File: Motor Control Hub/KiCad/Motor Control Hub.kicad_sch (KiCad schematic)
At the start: 6 parts, among them J2 GPIO, J3 Voltage Supply, J4 Motor Controllers

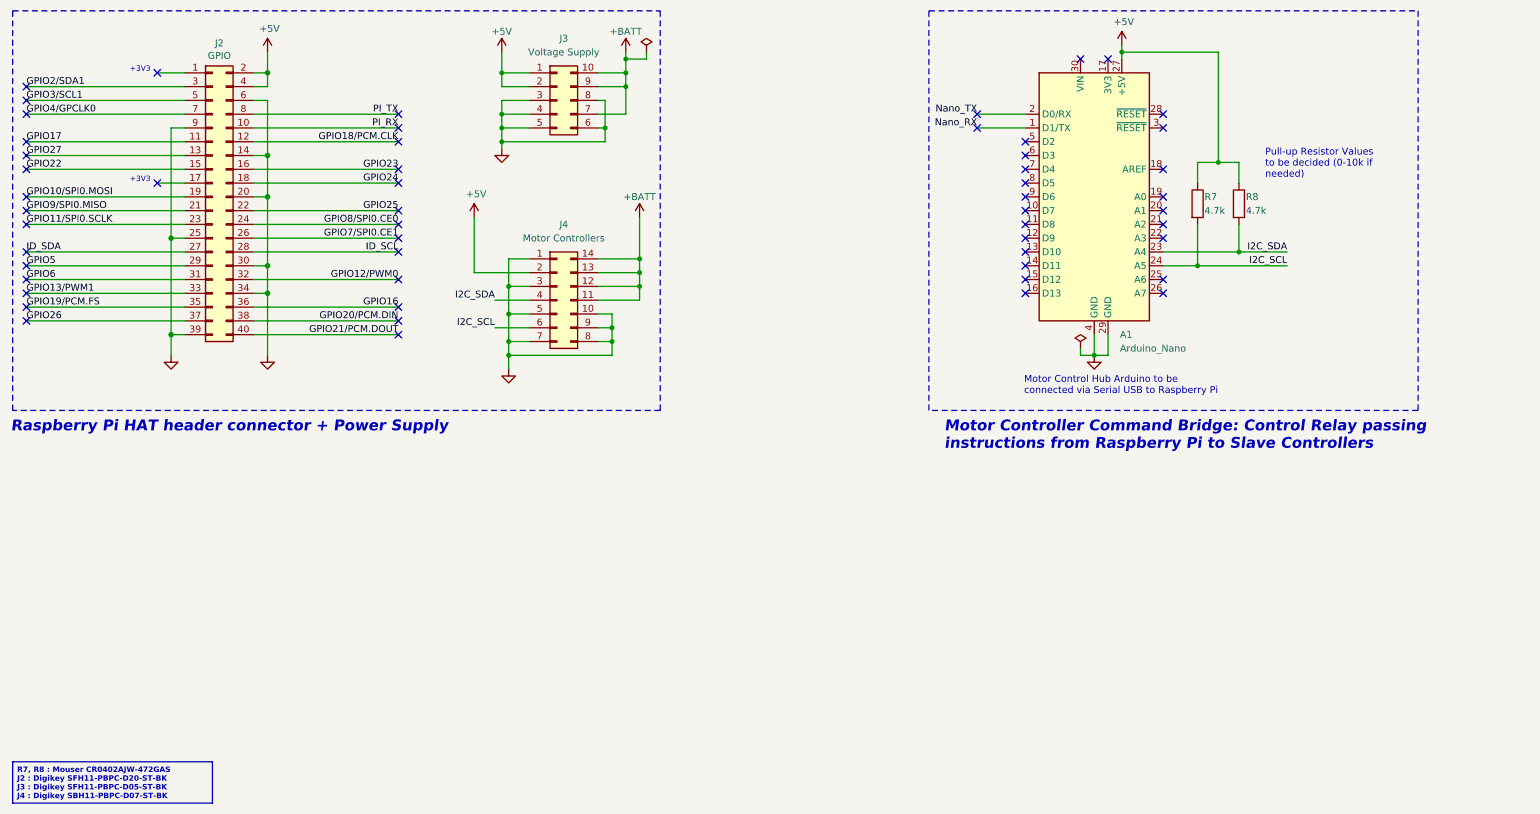
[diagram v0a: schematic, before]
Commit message: added encoders, slightly adjusted copper tracks
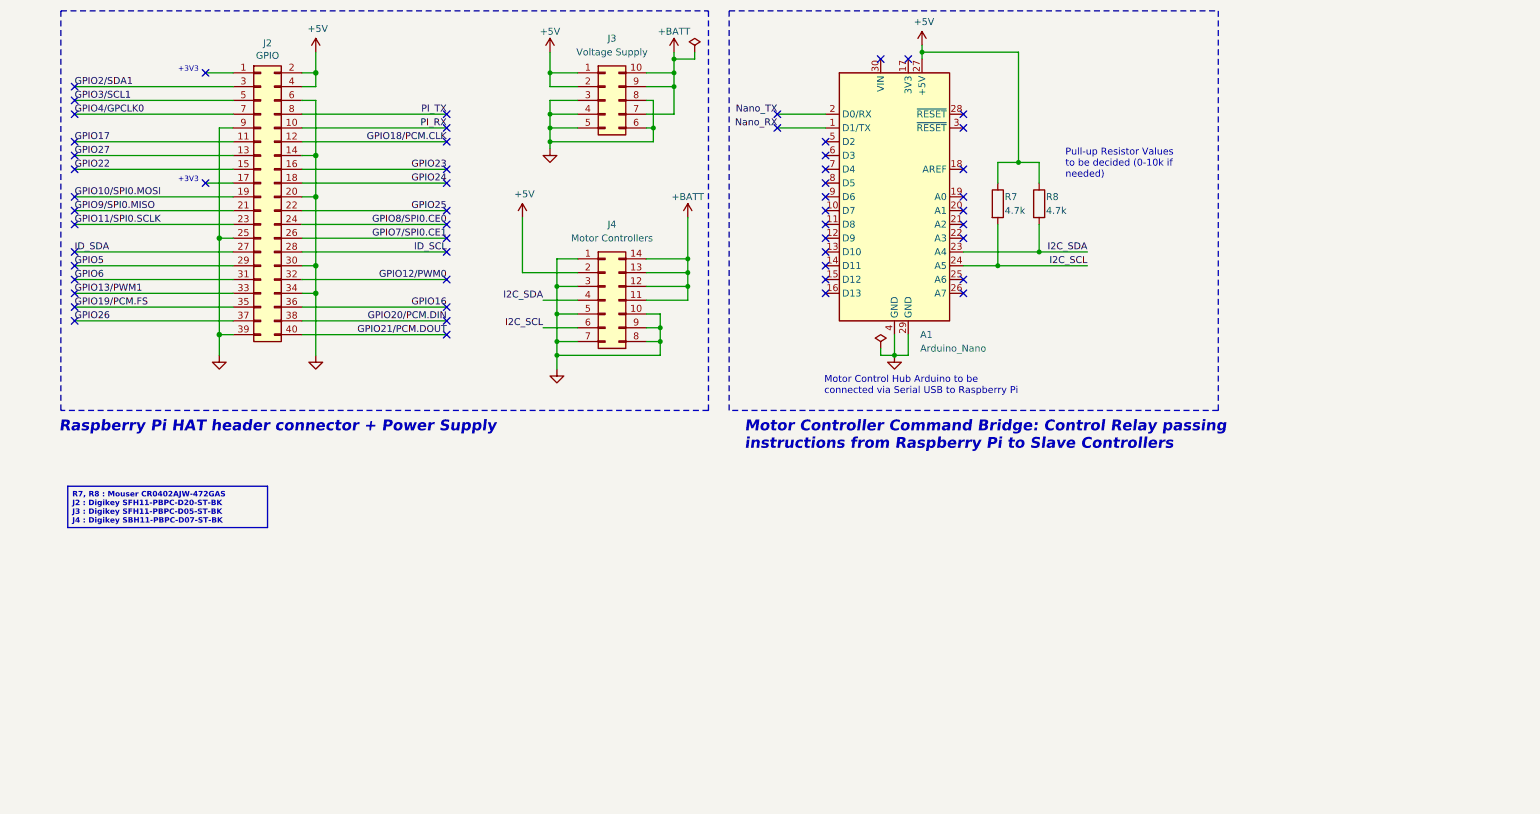
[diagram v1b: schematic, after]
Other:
- moved on the sheet: A1, J2, J3, J4, R7, R8
